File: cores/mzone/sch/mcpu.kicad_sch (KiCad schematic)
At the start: 36 parts

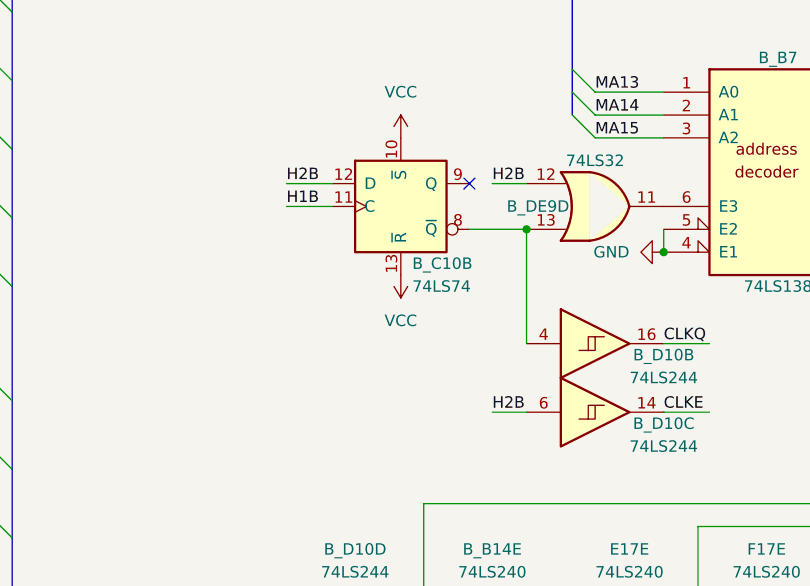
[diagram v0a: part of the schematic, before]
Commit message: mzone core
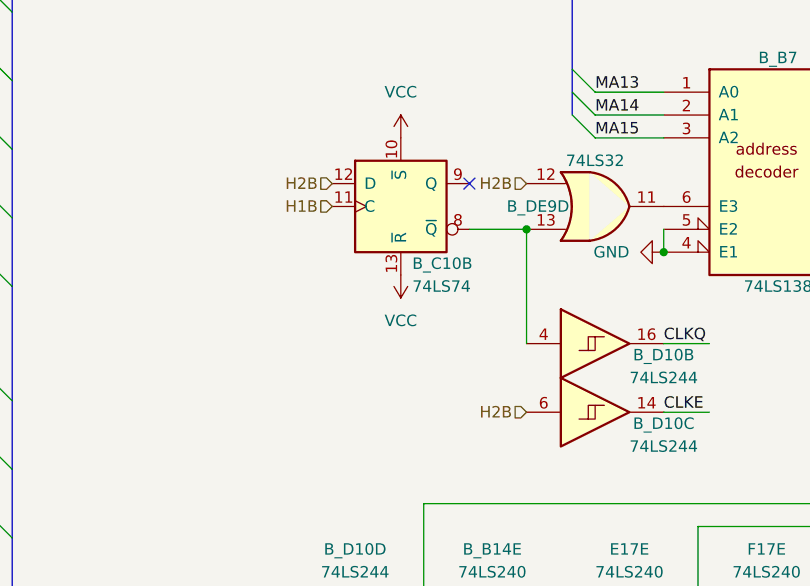
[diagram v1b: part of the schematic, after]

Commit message: mzone core
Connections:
- net ~{COLRAM'} renamed ~{CRAM'}
- net ~{COLRAM} renamed ~{CRAM}
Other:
- note added: "When ~{LACH} goes active, latch B_G9 goes inactive. When ~{LACH} goes inactive, B_G9 latches value and drives it if ~{CRAM} or ~{VRAM} are still active."
- note removed: "When ~{LACH} goes active, latch B_G9 goes inactive. When ~{LACH} goes inactive, B_G9 latches value and drives it if ~{COLRAM} or ~{VRAM} are still active."

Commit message: mzone core
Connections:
- net COIN_CNT'_1 renamed COIN_CNT'1
- net COIN_CNT'_2 renamed COIN_CNT'2
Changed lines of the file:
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@@
 	)
 	(bus_entry
+		(at 299.72 138.43)
+		(size 2.54 2.54)
+		(stroke
+			(width 0)
+			(type default)
+		)
+	)
+	(bus_entry
 		(at 195.58 195.58)
 		(size 2.54 2.54)
@@
 	)
 	(bus_entry
+		(at 299.72 130.81)
+		(size 2.54 2.54)
+		(stroke
+			(width 0)
+			(type default)
+		)
+	)
+	(bus_entry
 		(at 363.22 81.28)
 		(size -2.54 2.54)
@@
 		)
 	)
+	(wire
+		(pts
+			(xy 287.02 130.81) (xy 299.72 130.81)
+		)
+		(stroke
+			(width 0)
+			(type default)
+		)
+	)
 	(bus
 		(pts
@@
 		)
 	)
+	(bus
+		(pts
+			(xy 302.26 140.97) (xy 304.8 140.97)
+		)
+		(stroke
+			(width 0)
+			(type default)
+		)
+	)
 	(wire
 		(pts
@@
 	(wire
 		(pts
+			(xy 287.02 138.43) (xy 299.72 138.43)
+		)
+		(stroke
+			(width 0)
+			(type default)
+		)
+	)
+	(wire
+		(pts
 			(xy 279.4 29.21) (xy 285.75 29.21)
 		)
@@
 		)
 	)
+	(bus
+		(pts
+			(xy 302.26 133.35) (xy 302.26 140.97)
+		)
+		(stroke
+			(width 0)
+			(type default)
+		)
+	)
 	(wire
 		(pts
@@
 		)
 	)
+	(label "COIN_CNT'1"
+		(at 287.02 138.43 0)
+		(effects
+			(font
+				(size 1.27 1.27)
+			)
+			(justify left bottom)
+		)
+	)
 	(label "MD'5"
 		(at 181.61 31.75 0)
@@
 		)
 	)
+	(label "COIN_CNT'2"
+		(at 287.02 130.81 0)
+		(effects
+			(font
+				(size 1.27 1.27)
+			)
+			(justify left bottom)
+		)
+	)
 	(label "MA9"
 		(at 331.47 50.8 0)
@@
 		)
 	)
-	(hierarchical_label "COIN_CNT'_2"
-		(shape output)
-		(at 287.02 130.81 0)
-		(effects
-			(font
-				(size 1.27 1.27)
-			)
-			(justify left)
-		)
-	)
 	(hierarchical_label "~{H2}"
 		(shape input)
@@
 		)
 	)
-	(hierarchical_label "COIN_CNT'_1"
-		(shape output)
-		(at 287.02 138.43 0)
-		(effects
-			(font
-				(size 1.27 1.27)
-			)
-			(justify left)
-		)
-	)
 	(hierarchical_label "H2B"
 		(shape input)
@@
 		(effects
 			(font
+				(size 1.27 1.27)
+			)
+			(justify left)
+		)
+	)
+	(hierarchical_label "COIN_CNT'[2..1]"
+		(shape output)
+		(at 304.8 140.97 0)
+		(effects
+			(font

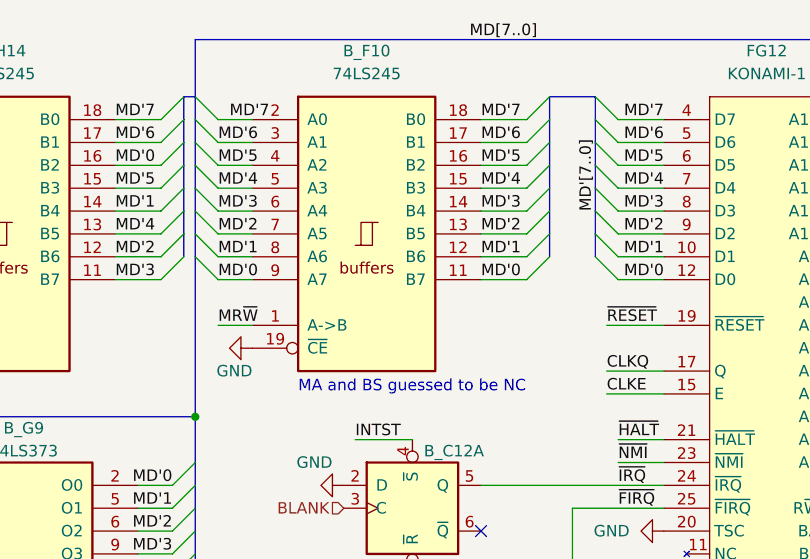
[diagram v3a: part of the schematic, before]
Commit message: mzone core
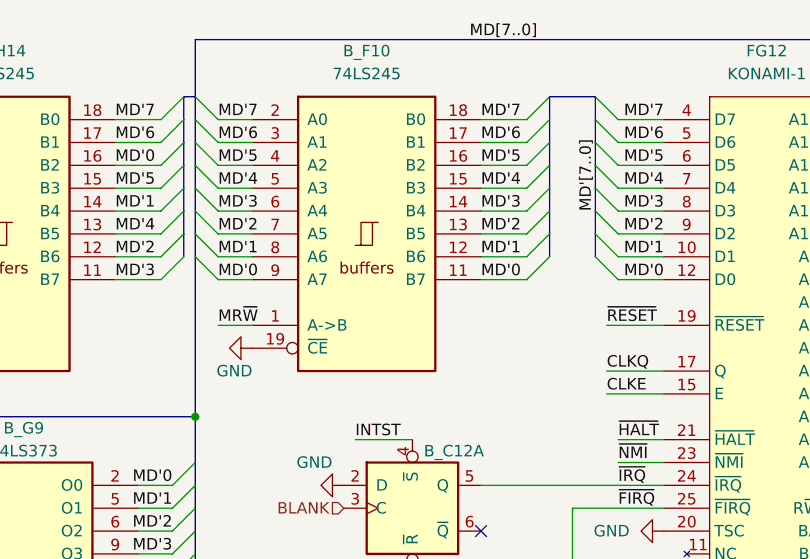
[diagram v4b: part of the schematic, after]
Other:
- note removed: "MA and BS guessed to be NC"
